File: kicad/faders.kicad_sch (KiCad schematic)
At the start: 122 parts, among them J14 Conn_01x06_Socket, J15 Conn_01x06_Socket, J16 Conn_01x06_Socket, J18 Conn_01x05_Socket, J19 Conn_01x06_Socket, J20 Conn_01x05_Socket, J21 Conn_01x06_Socket, J31 Conn_01x06_Socket, J32 Conn_01x06_Socket, J33 Conn_01x05_Socket, J34 Conn_01x05_Socket, J36 Conn_01x06_Socket, SW1 RotaryEncoder_Switch, SW10 RotaryEncoder_Switch, SW11 SW_SPST, SW12 SW_SPST, SW13 SW_SPST, SW14 SW_SPST, SW15 SW_SPST, SW16 SW_SPST, SW17 SW_SPST, SW18 SW_SPST, SW19 SW_SPST, SW2 RotaryEncoder_Switch, SW20 SW_SPST, SW21 SW_SPST, SW22 SW_SPST, SW23 SW_SPST, SW24 SW_SPST, SW25 SW_SPST, SW3 RotaryEncoder_Switch, SW4 RotaryEncoder_Switch, SW5 RotaryEncoder_Switch, SW6 RotaryEncoder_Switch, SW7 RotaryEncoder_Switch, SW8 RotaryEncoder_Switch, SW9 RotaryEncoder_Switch, U1 LS30, U10 MCP23S17_SO, U11 MCP23S17_SO, U12 MCP23S17_SO, U13 MCP23S17_SO, U14 MCP23S17_SO, U15 MCP3008, U16 LS30, U17 PCA9635, U18 DRV8210, U19 DRV8210, U2 LS30, U20 DRV8210, U21 DRV8210, U22 DRV8210, U23 LS30, U24 LM4040D33, U3 LS30, U4 LS30, U5 LS30, U6 LS30, U7 LS30, U8 LS30, U9 MTCH105

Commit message: update kicad files
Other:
- note added: "^ bank/bpm screen (fb0 for bank, pb1 for bpm)"

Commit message: feat(schem): started implementing the rp2040 on each wing
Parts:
- removed J16, J36: Conn_01x06_Socket, Connector_JST:JST_XH_B6B-XH-A_1x06_P2.50mm_Vertical, symbol Connector:Conn_01x06_Socket
- removed J33, J34: Conn_01x05_Socket, Connector_JST:JST_XH_B5B-XH-A_1x05_P2.50mm_Vertical, symbol Connector:Conn_01x05_Socket
- removed U10: MCP23S17_SO, Package_SO:SOIC-28W_7.5x17.9mm_P1.27mm, symbol Interface_Expansion:MCP23S17_SO
- added C100, C101, C102, C103, C94, C95, C98, C99: 100n, Capacitor_SMD:C_0603_1608Metric_Pad1.08x0.95mm_HandSolder, symbol Device:C
- added C80, C90: 27p, Capacitor_SMD:C_0603_1608Metric_Pad1.08x0.95mm_HandSolder, symbol Device:C
- added C96, C97: 1u, Capacitor_SMD:C_0603_1608Metric_Pad1.08x0.95mm_HandSolder, symbol Device:C
- added J16: Conn_02x03_Counter_Clockwise, Connector_PinHeader_2.54mm:PinHeader_2x03_P2.54mm_Vertical, symbol Connector_Generic:Conn_02x03_Counter_Clockwise
- added R46: R, Resistor_SMD:R_0603_1608Metric_Pad0.98x0.95mm_HandSolder, symbol Device:R
- added R54: NFIT, Resistor_SMD:R_0603_1608Metric_Pad0.98x0.95mm_HandSolder, symbol Device:R
- added R55, R59: 1K, Resistor_SMD:R_0603_1608Metric_Pad0.98x0.95mm_HandSolder, symbol Device:R
- added R56: 10K, Resistor_SMD:R_0603_1608Metric_Pad0.98x0.95mm_HandSolder, symbol Device:R
- added U10: LM4040D33, Package_TO_SOT_SMD:SOT-23, symbol Reference_Voltage:LM4040DBZ-2.0
- added U46: AT25SF081-SSHD-X, Package_SO:SOIC-8_3.9x4.9mm_P1.27mm, symbol Memory_Flash:AT25SF081-SSHD-X
- added U47: RP2040, Package_DFN_QFN:QFN-56-1EP_7x7mm_P0.4mm_EP3.2x3.2mm, symbol MCU_RaspberryPi:RP2040
- added Y3: 12Mhz, Crystal:Crystal_SMD_HC49-SD, symbol Device:Crystal
- C37: value 1u -> 2u2
- C45, C46, U14: now not fitted
- U13: footprint Package_SO:SOIC-18W_7.5x11.6mm_P1.27mm -> Package_SO:SOIC-28W_7.5x17.9mm_P1.27mm; symbol Interface_Expansion:MCP23008-xSO -> Interface_Expansion:MCP23S17_SO
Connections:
- net +E3V3: now also U13.9 (VDD); no longer U13.18 (VCC)
- net +F3V3: now also C100.1, C101.1, C102.1, C103.1, C97.1, C98.1, C99.1, J16.1 (Pin_1), R46.1, R54.1, R56.1, U46.8 (VCC), U47.1 (IOVDD), U47.10 (IOVDD), U47.22 (IOVDD), U47.33 (IOVDD), U47.42 (IOVDD), U47.44 (VREG_IN), U47.48 (USB_VDD), U47.49 (IOVDD)
- net B00F: no longer U14.4 (GPB3)
- net B01F: no longer U14.5 (GPB4)
- net B02F: no longer U14.6 (GPB5)
- net B03F: no longer U14.7 (GPB6)
- net B04F: no longer U14.8 (GPB7)
- net B09: now also U13.4 (GPB3); no longer U13.13 (GP3)
- net B14: now also U13.5 (GPB4); no longer U13.14 (GP4)
- net CS_U13-ENC: now also U13.11 (~{CS}); no longer U13.7 (~{CS})
- net EGND: now also U13.10 (VSS), U13.15 (A0), U13.16 (A1), U13.17 (A2); no longer U13.4 (A1), U13.5 (A0), U13.9 (VSS)
- net FGND: now also C100.2, C101.2, C102.2, C103.2, C80.1, C90.1, C94.2, C95.2, C96.2, C97.2, C98.2, C99.2, J16.2 (Pin_2), U10.2 (A), U46.4 (GND), U47.19 (TESTEN), U47.57 (GND)
- net INT_U13-ENC: now also U13.19 (INTB), U13.20 (INTA); no longer U13.8 (INT)
- net T0: no longer U14.25 (GPA4)
- net T1: no longer U14.24 (GPA3)
- net T2: no longer U14.23 (GPA2)
- net T3: no longer U14.22 (GPA1)
- net T4: no longer U14.21 (GPA0)
- net ~{ERST}: now also U13.18 (~{RESET}); no longer U13.6 (~{RESET})
- net at U23.5 (SWO): now also U13.8 (GPB7); no longer U13.17 (GP7)
- net at U23.6 (D): now also U13.7 (GPB6); no longer U13.16 (GP6)
- net at U23.7 (P): now also U13.6 (GPB5); no longer U13.15 (GP5)
- net at U16.5 (SWO): now also U13.3 (GPB2); no longer U13.12 (GP2)
- net at U16.6 (D): now also U13.2 (GPB1); no longer U13.11 (GP1)
- net at U16.7 (P): now also U13.1 (GPB0); no longer U13.10 (GP0)
- net SPI0MISO-ENC renamed SPI1MISO-ENC
- net SPI1MISO-ENC: now also U13.14 (SO); no longer U13.3 (SO)
- net SPI0MOSI-ENC renamed SPI1MOSI-ENC
- net SPI1MOSI-ENC: now also U13.13 (SI); no longer U13.2 (SI)
- net SPI0SCK-ENC renamed SPI1SCK-ENC
- net SPI1SCK-ENC: now also U13.12 (SCK); no longer U13.1 (SCK)
- new net: C90.2, R59.1, Y3.1
- new net: C80.2, U47.20 (XIN), Y3.2
- new net: R59.2, U47.21 (XOUT)
- new net +1V1: C94.1, C95.1, C96.1, U47.23 (DVDD), U47.45 (VREG_VOUT), U47.50 (DVDD)
- new net F_BOOTSEL: J16.3 (Pin_3), R55.2
- new net F_QSPI_CS: R54.2, R55.1, U46.1 (~{CS}), U47.56 (QSPI_SCS)
- new net F_QSPI_SCL: U46.6 (SCK), U47.52 (QSPI_SCLK)
- new net F_QSPI_SD0: U46.5 (SI/IO0), U47.53 (QSPI_SD0)
- new net F_QSPI_SD1: U46.2 (SO/IO1), U47.55 (QSPI_SD1)
- new net F_QSPI_SD2: U46.3 (~{WP}/IO2), U47.54 (QSPI_SD2)
- new net F_QSPI_SD3: U46.7 (~{HOLD}/IO3), U47.51 (QSPI_SD3)
- new net F_RESET_RP2: J16.4 (Pin_4), R56.2, U47.26 (RUN)
- new net F_RP2_VREF: R46.2, U10.1 (K), U47.43 (ADC_AVDD)
- new net F_SWCLK: J16.6 (Pin_6), U47.24 (SWCLK)
- new net F_SWDIO: J16.5 (Pin_5), U47.25 (SWD)
- no-connect marks 6 -> 8
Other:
- note added: "(10K)"
- note added: "SW-DEBUG-HEADER"
- note added: "TODO: Display backlight drivers"
- note added: "TODO: Reset system"
- note added: "TODO: add mainboard connections"
- note added: "VALUE R32? 3v0/3v3 reference"
- note added: "place c5 close to pin 45 of rp2040"
- note added: "place c8 close to pin 44 of rp2040"
- note removed: "Main board conns"
- note removed: "^ bank/bpm screen (fb0 for bank, pb1 for bpm)"
- moved on the sheet: C35, C36, C39, C40, C41, C42, C43, C44, C47, C48, C51, C52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

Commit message: changed some more of the schematic
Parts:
- C45, C46, U14: now fitted
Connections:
- no-connect marks 8 -> 2
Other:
- note added: "half use pwm. other half are on/off"
- moved on the sheet: C100, C101, C102, C103, C37, C38, C80, C90, C94, C95, C96, C97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

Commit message: feat(sch): mostly figured uit pinout for rp2040 and some other small edits
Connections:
- net B00F: now also U14.4 (GPB3)
- net B01F: now also U14.5 (GPB4)
- net B02F: now also U14.6 (GPB5)
- net B03F: now also U14.7 (GPB6)
- net B04F: now also U14.8 (GPB7)
- net CS_U11: now also J19.2 (Pin_2), U47.6 (GPIO4)
- net CS_U12: now also J19.4 (Pin_4), U47.4 (GPIO2)
- net CS_U13: now also J19.6 (Pin_6), U47.2 (GPIO0)
- net EGND: no longer J20.1 (Pin_1)
- net FSCL: now also U47.9 (GPIO7)
- net FSDA: now also U47.8 (GPIO6)
- net FSPI0MISO: now also U47.35 (GPIO23)
- net FSPI0MOSI: now also U47.31 (GPIO20)
- net FSPI0SCL: now also U47.34 (GPIO22)
- net FSPI1DC: now also U47.41 (GPIO29_ADC3)
- net FSPI1MISO: now also U47.40 (GPIO28_ADC2)
- net FSPI1MOSI: now also U47.39 (GPIO27_ADC1)
- net FSPI1SCL: now also U47.38 (GPIO26_ADC0)
- net T0: now also U14.25 (GPA4)
- net T1: now also U14.24 (GPA3)
- net T2: now also U14.23 (GPA2)
- net T3: now also U14.22 (GPA1)
- net T4: now also U14.21 (GPA0)
- net U17~{OE}: now also U47.11 (GPIO8)
- net INT_U11: now reaches J19.1 (Pin_1)
- net INT_U11: now also U47.7 (GPIO5)
- net INT_U12: now reaches J19.3 (Pin_3)
- net INT_U12: now also U47.5 (GPIO3)
- net INT_U13: now reaches J19.5 (Pin_5)
- net INT_U13: now also U47.3 (GPIO1)
- net FXIN: now reaches C80.2, U47.20 (XIN), Y3.2
- net FXOUT: now reaches R59.2, U47.21 (XOUT)
- net CS_WING: now reaches U47.32 (GPIO21)
- no-connect marks 2 -> 8
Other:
- moved on the sheet: J18, J19, J20, J21

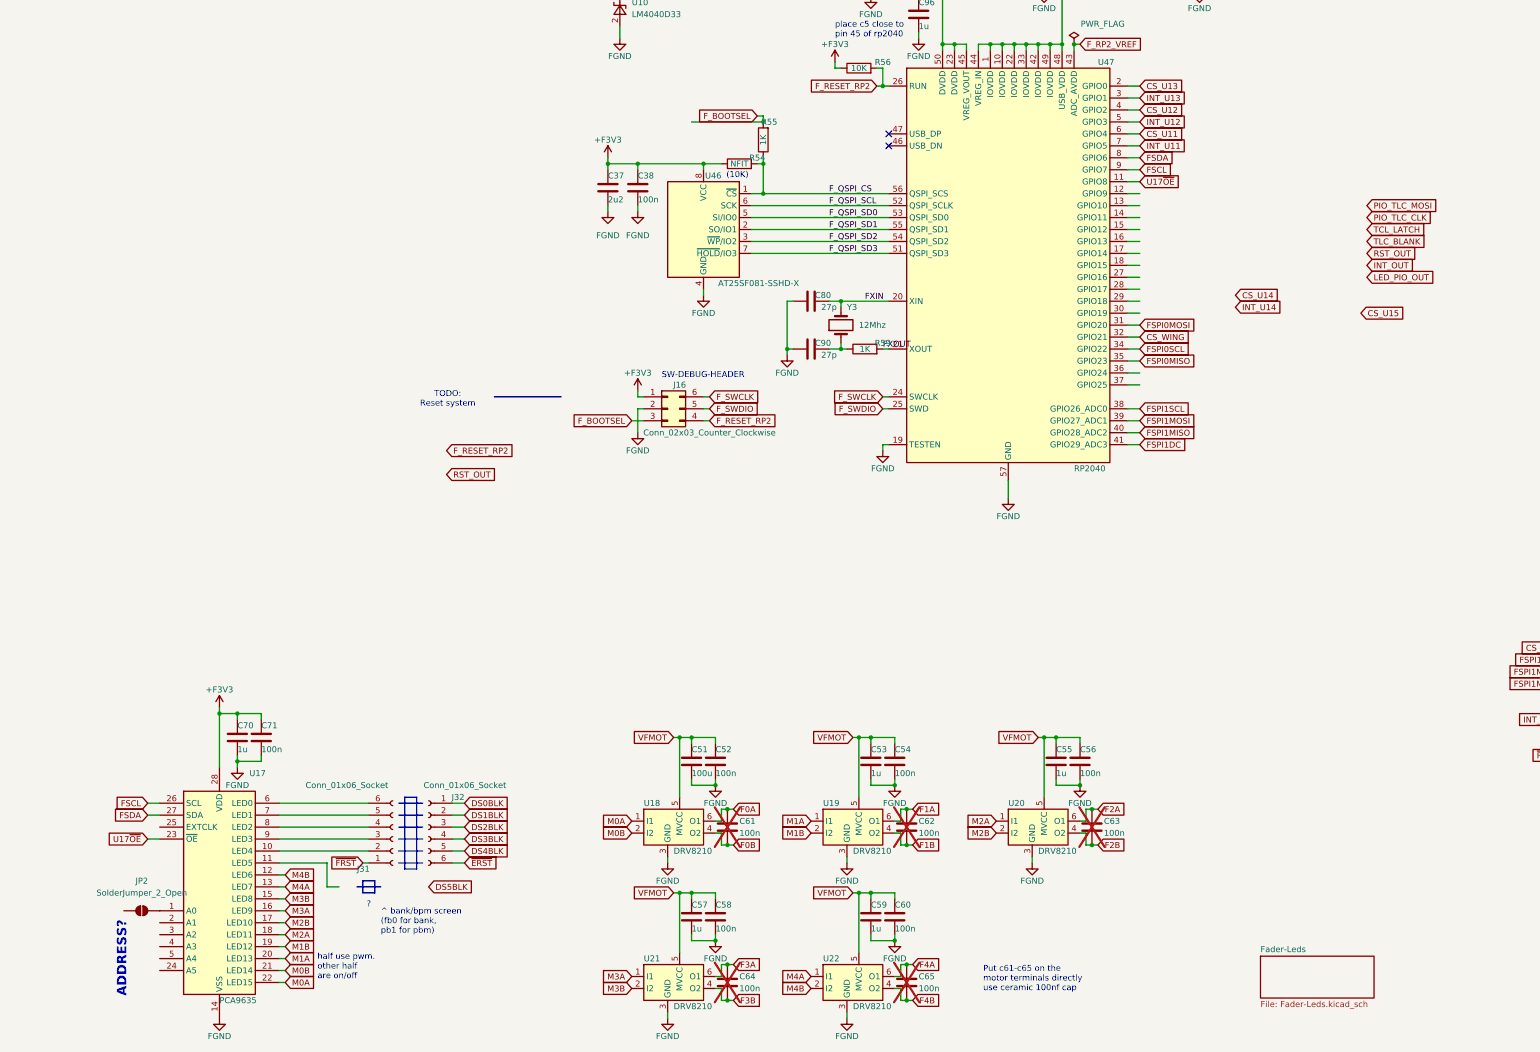
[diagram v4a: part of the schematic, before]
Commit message: feat(pcb): routing tracks from mcu to pheriperals
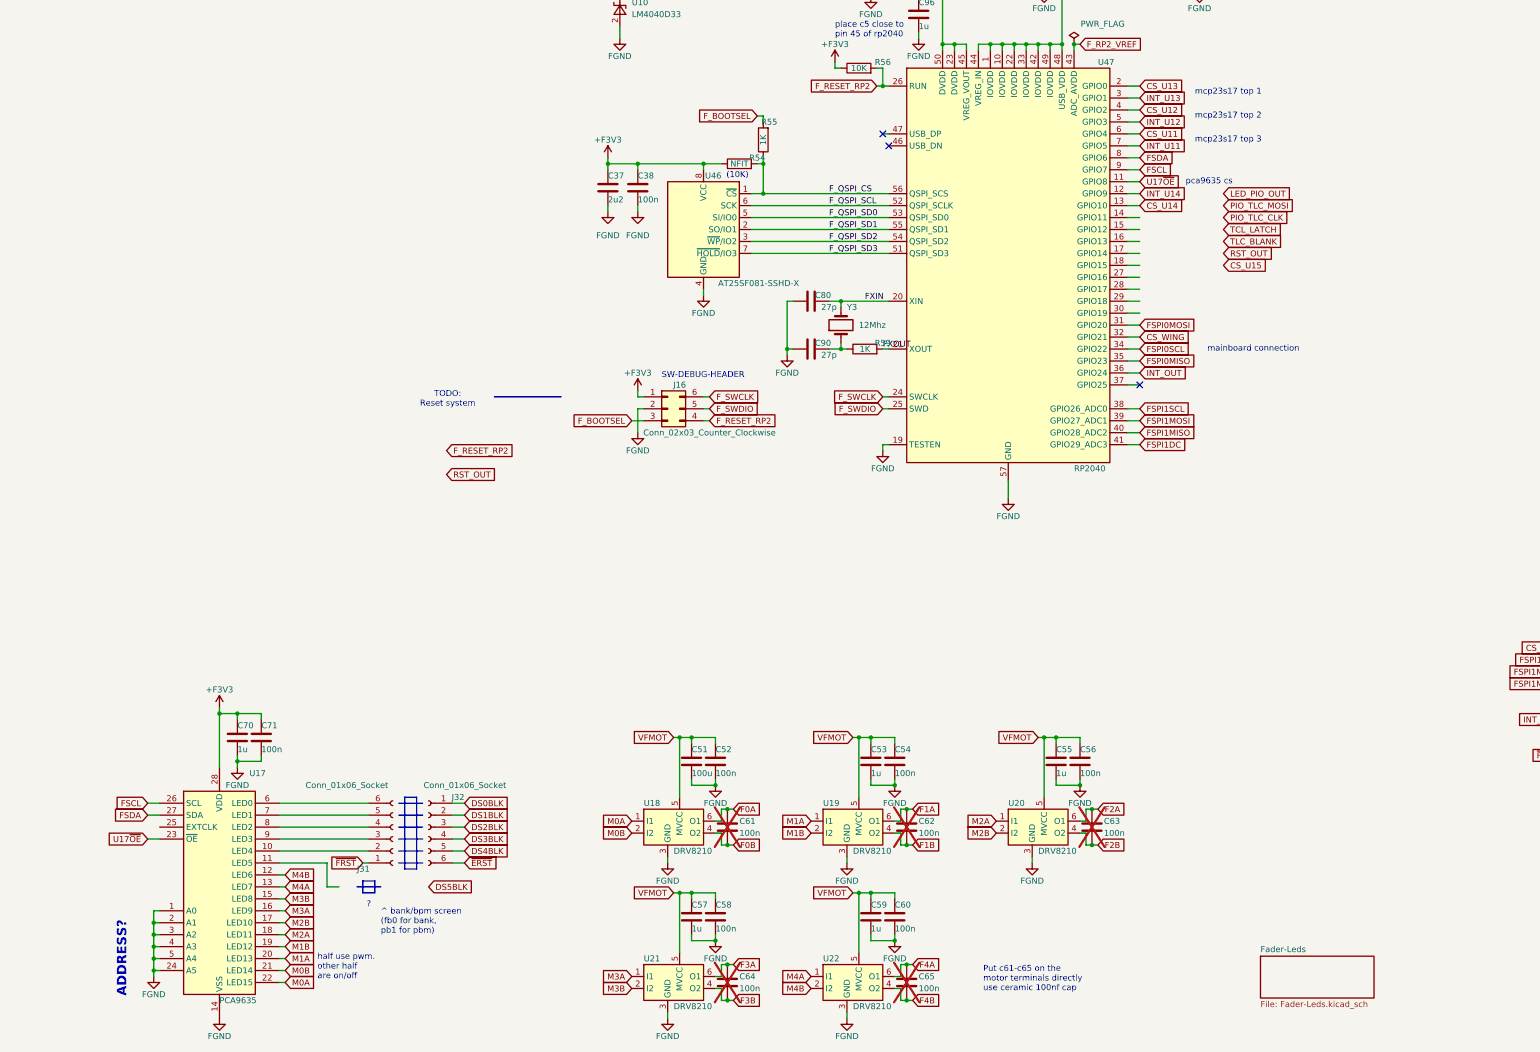
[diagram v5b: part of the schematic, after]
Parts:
- removed JP2: SolderJumper_2_Open, Jumper:SolderJumper-2_P1.3mm_Open_RoundedPad1.0x1.5mm, symbol Jumper:SolderJumper_2_Open
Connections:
- net CS_U14: now also U47.13 (GPIO10)
- net FGND: now also U17.1 (A0), U17.2 (A1), U17.24 (A5), U17.3 (A2), U17.4 (A3), U17.5 (A4)
- net INT_OUT: now also U47.36 (GPIO24)
- net INT_U14: now also U47.12 (GPIO9)
- no-connect marks 8 -> 9
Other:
- note added: "mainboard connection"
- note added: "mcp23s17 top 1"
- note added: "mcp23s17 top 2"
- note added: "mcp23s17 top 3"
- note added: "pca9635 cs"

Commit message: continued work on fader pcb and redid all references more logicly
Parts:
- removed C103: 100n, Capacitor_SMD:C_0603_1608Metric_Pad1.08x0.95mm_HandSolder, symbol Device:C
- removed R46: R, Resistor_SMD:R_0603_1608Metric_Pad0.98x0.95mm_HandSolder, symbol Device:R
- removed U10: LM4040D33, Package_TO_SOT_SMD:SOT-23, symbol Reference_Voltage:LM4040DBZ-2.0
- removed U18, U19, U20, U21, U22: DRV8210, personal:SOT-6, symbol Personal:DRV8210
- added R321, R322, R323, R324, R325: 80K, Resistor_SMD:R_0603_1608Metric_Pad0.98x0.95mm_HandSolder, symbol Device:R
- added U308, U309, U310, U311, U312: DRV8871DDA, Package_SO:Texas_HTSOP-8-1EP_3.9x4.9mm_P1.27mm_EP2.95x4.9mm_Mask2.4x3.1mm_ThermalVias, symbol Driver_Motor:DRV8871DDA
- C53, C55, C57, C59: value 1u -> 100u
- renumbered C94 to C303, C95 to C304, C97 to C305, C98 to C306, C99 to C307, C100 to C308, C101 to C309, C102 to C310, C96 to C312, C37 to C336, C38 to C337, C80 to C338, C90 to C339, C39 to C402, C40 to C403, C41 to C404, C42 to C405, C43 to C406, C44 to C407, J16 to J301, R59 to R301, R54 to R302, R55 to R303, R56 to R304, SW1 to SW400, SW2 to SW401, SW3 to SW402, SW4 to SW403, SW5 to SW404, SW6 to SW405, SW7 to SW406, SW8 to SW407, SW9 to SW408, SW10 to SW409, SW16 to SW410, SW17 to SW411, SW18 to SW412, SW19 to SW413, SW20 to SW414, SW21 to SW415, SW22 to SW416, SW23 to SW417, SW24 to SW418, SW25 to SW419, U47 to U301, U46 to U302, U11 to U401, U12 to U402, U13 to U403, U4 to U404, U1 to U405, U8 to U406, U5 to U407, U16 to U408, U3 to U409, U2 to U410, U7 to U411, U6 to U412, U23 to U413, Y3 to X301
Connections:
- net F_RP2_VREF is gone; now on net +F3V3: U301.43 (ADC_AVDD)
- net DS0CS: now also U403.24 (GPA3)
- net DS1CS: now also U403.25 (GPA4)
- net DS2CS: now also U403.26 (GPA5)
- net DS3CS: now also U403.27 (GPA6)
- net DS4CS: now also U403.28 (GPA7)
- net EGND: now also J20.1 (Pin_1)
- net F0A: now also C61.2, U308.8 (OUT2); no longer C61.1
- net F0B: now also C61.1, U308.6 (OUT1); no longer C61.2
- net F1A: now also C62.2, U309.8 (OUT2); no longer C62.1
- net F1B: now also C62.1, U309.6 (OUT1); no longer C62.2
- net F2A: now also C63.2, U310.8 (OUT2); no longer C63.1
- net F2B: now also C63.1, U310.6 (OUT1); no longer C63.2
- net F3A: now also C64.2, U311.8 (OUT2); no longer C64.1
- net F3B: now also C64.1, U311.6 (OUT1); no longer C64.2
- net F4A: now also C65.2, U312.8 (OUT2); no longer C65.1
- net F4B: now also C65.1, U312.6 (OUT1); no longer C65.2
- net FGND: now also R321.1, R322.1, R323.1, R324.1, R325.1, U308.1 (GND), U308.7 (GND), U308.9 (GND), U309.1 (GND), U309.7 (GND), U309.9 (GND), U310.1 (GND), U310.7 (GND), U310.9 (GND), U311.1 (GND), U311.7 (GND), U311.9 (GND), U312.1 (GND), U312.7 (GND), U312.9 (GND)
- net M0A: now also U308.2 (IN2)
- net M0B: now also U308.3 (IN1)
- net M1A: now also U309.2 (IN2)
- net M1B: now also U309.3 (IN1)
- net M2A: now also U310.2 (IN2)
- net M2B: now also U310.3 (IN1)
- net M3A: now also U311.2 (IN2)
- net M3B: now also U311.3 (IN1)
- net M4A: now also U312.2 (IN2)
- net M4B: now also U312.3 (IN1)
- net VFMOT: now also U308.5 (VM), U309.5 (VM), U310.5 (VM), U311.5 (VM), U312.5 (VM)
- new net: R322.2, U309.4 (ILIM)
- new net: R325.2, U312.4 (ILIM)
- new net: R324.2, U311.4 (ILIM)
- new net: R321.2, U308.4 (ILIM)
- new net: R323.2, U310.4 (ILIM)
- no-connect marks 9 -> 12
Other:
- note added: "ADDRESS? Nope"
- note added: "Put c329-c333 on the motor terminals/faders directly use ceramic 100nf cap c320,322,324,326,328 should be ceramic"
- note added: "TODO: add display backlight drivers"
- note added: "TODO: add mainboard connections j3 j4"
- note removed: "ADDRESS?"
- note removed: "Put c61-c65 on the motor terminals directly use ceramic 100nf cap"
- note removed: "TODO: Display backlight drivers"
- note removed: "TODO: add mainboard connections"
- note removed: "VALUE R32? 3v0/3v3 reference"
- moved on the sheet: C338, C339, C51, C52, C53, C54, C55, C56, C57, C58, C59, C60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

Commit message: finish updateing all references, add schematic pdf and some more progress
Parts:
- renumbered C72 to C301, C66 to C302, C35 to C313, C36 to C314, C47 to C315, C48 to C316, C70 to C317, C71 to C318, C51 to C319, C52 to C320, C53 to C321, C54 to C322, C55 to C323, C56 to C324, C57 to C325, C58 to C326, C59 to C327, C60 to C328, C61 to C329, C62 to C330, C63 to C331, C64 to C332, C65 to C333, C45 to C334, C46 to C335, DS1 to DS301, DS2 to DS302, DS3 to DS303, DS4 to DS304, DS5 to DS305, J15 to J302, J14 to J303, J19 to J307, J21 to J308, J18 to J309, J20 to J310, J31 to J311, J32 to J312, MF1 to MF301, MF2 to MF302, MF3 to MF303, MF4 to MF304, MF5 to MF305, R36 to R305, R37 to R306, R38 to R307, R39 to R308, R40 to R309, R45 to R310, R44 to R311, R43 to R312, R42 to R313, R41 to R314, R22 to R315, R24 to R316, R25 to R317, R26 to R318, R27 to R319, R33 to R320, RV1 to RV301, SW11 to SW300, SW12 to SW301, SW13 to SW302, SW14 to SW303, SW15 to SW304, U9 to U303, U15 to U304, U24 to U305, U17 to U306, U14 to U307
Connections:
- net +F-3V3 is gone; now on net +F3V3: RV301.3
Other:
- note added: "TODO: move display and drive circuits to 4xx pcb. update references on all schematic and pcb's"
- moved on the sheet: C305, C306, C307, C308, C309, C310
